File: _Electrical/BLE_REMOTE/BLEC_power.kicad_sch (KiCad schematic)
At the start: 37 parts, among them J1 USBC, J4 Battery, Q1 RE1C002UNTCL, Q2 IRLML6244, SW1 SW_Push, U2 BQ24232RGTR, U3 MCP65R41, U4 MIC5528-3.3YMX-TR

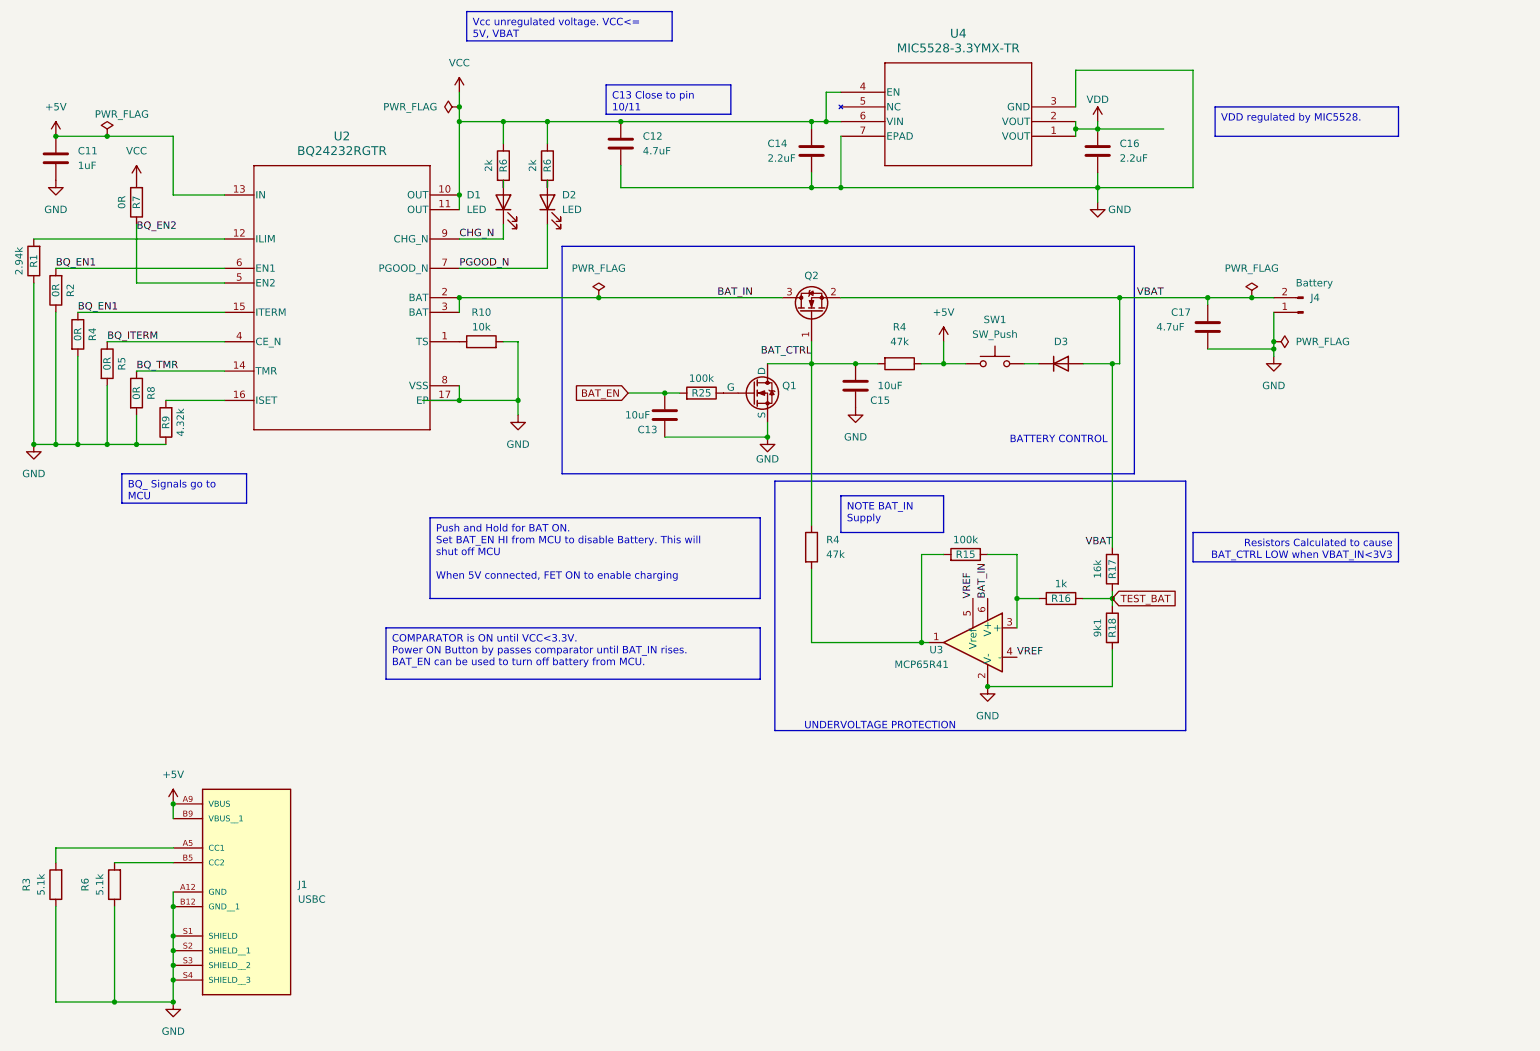
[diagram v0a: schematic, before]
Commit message: Added simulation and updated power button
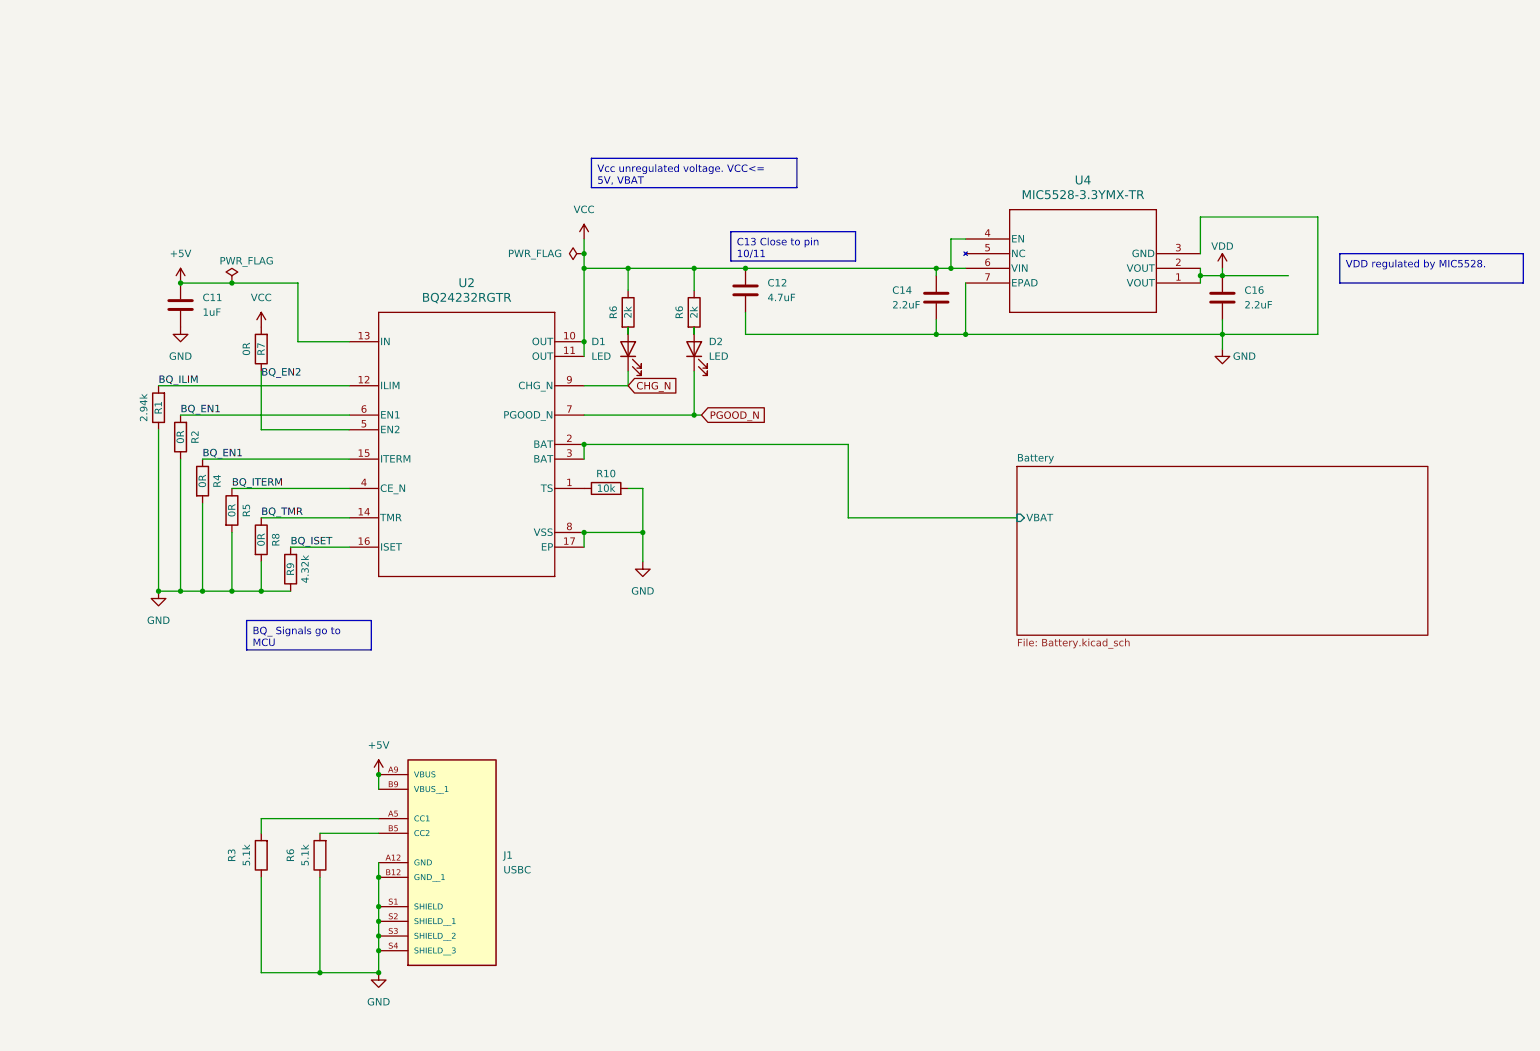
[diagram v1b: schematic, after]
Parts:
- removed C13, C15: 10uF, Capacitor_SMD:C_0402_1005Metric_Pad0.74x0.62mm_HandSolder, symbol Device:C
- removed C17: 4.7uF, Capacitor_SMD:C_0805_2012Metric_Pad1.18x1.45mm_HandSolder, symbol Device:C
- removed D3: 1N4148WX-TP, _Parts:CR_SOD323_MCC-L, symbol Device:D
- removed J4: Battery, _Parts:2pad_conn_sm, symbol Connector:Conn_01x02_Pin
- removed Q1: RE1C002UNTCL, _Parts:DIO_RB558WMF_ROM, symbol Simulation_SPICE:NMOS
- removed Q2: IRLML6244, Package_TO_SOT_SMD:SOT-23, symbol Transistor_FET:IRLML6244
- removed R15, R25: 100k, Resistor_SMD:R_0402_1005Metric_Pad0.72x0.64mm_HandSolder, symbol Device:R
- removed R16: 1k, Resistor_SMD:R_0402_1005Metric_Pad0.72x0.64mm_HandSolder, symbol Device:R
- removed R17: 16k, Resistor_SMD:R_0402_1005Metric_Pad0.72x0.64mm_HandSolder, symbol Device:R
- removed R18: 9k1, Resistor_SMD:R_0402_1005Metric_Pad0.72x0.64mm_HandSolder, symbol Device:R
- removed R4 (x2): 47k, Resistor_SMD:R_0402_1005Metric_Pad0.72x0.64mm_HandSolder, symbol Device:R
- removed SW1: SW_Push, symbol Switch:SW_Push
- removed U3: MCP65R41, Package_TO_SOT_SMD:SOT-23-6, symbol Comparator:MCP65R41
- J1: footprint USB4125-GF-A_REVA2:GCT_USB4125-GF-A_REVA2 -> _Parts:GCT_USB4125-GF-A_REVA2
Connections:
- net BQ_ISET: now reaches R9.2, U2.16 (ISET)
- net BQ_ILIM: now reaches R1.2, U2.12 (ILIM)
- net BAT_IN renamed Battery/VBAT
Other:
- added sheet Battery (Battery.kicad_sch)
- note removed: "BATTERY CONTROL"
- note removed: "UNDERVOLTAGE PROTECTION"
- moved on the sheet: C11, C12, C14, C16, D1, D2, J1, R1, R10, R2, R3, R4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

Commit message: started PCB design
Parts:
- removed J1: USBC, _Parts:GCT_USB4125-GF-A_REVA2, symbol USB4125-GF-A_REVA2:USB4125-GF-A_REVA2
- removed R3, R6: 5.1k, Resistor_SMD:R_0402_1005Metric_Pad0.72x0.64mm_HandSolder, symbol Device:R
- renumbered C14 to C13, C16 to C14, R4 to R3, R5 to R4, R7 to R5, R8 to R6, R9 to R7, U4 to U3
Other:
- added sheet USBC (USBC.kicad_sch)
- moved on the sheet: R10

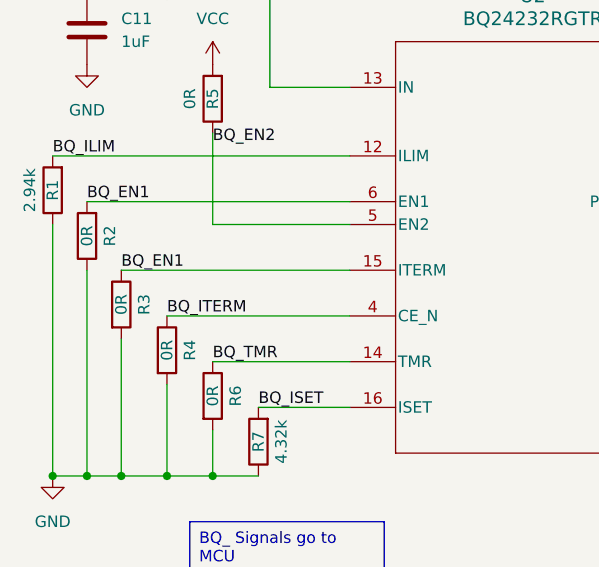
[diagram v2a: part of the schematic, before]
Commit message: PCB parts placed
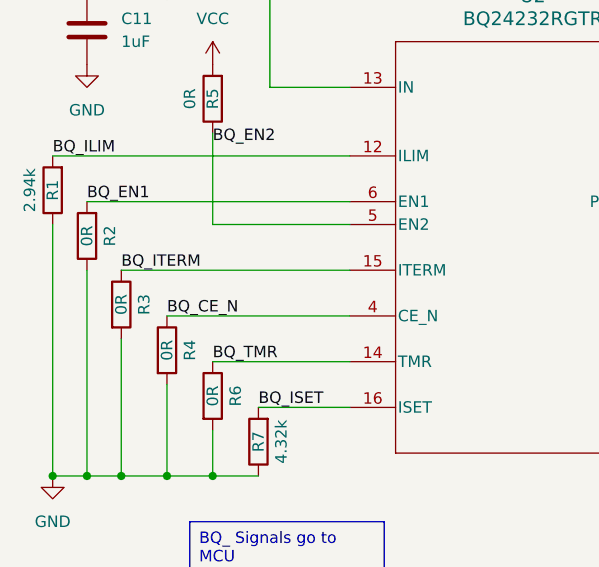
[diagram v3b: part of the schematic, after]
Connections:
- net BQ_EN1: no longer R3.1, U2.15 (ITERM)
- net BQ_ITERM: now also R3.1, U2.15 (ITERM); no longer R4.1, U2.4 (CE_N)
- new net BQ_CE_N: R4.1, U2.4 (CE_N)
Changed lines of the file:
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@@
     (effects (font (size 1.27 1.27)) (justify left bottom))
   )
-  (label "BQ_ITERM" (at 54.61 100.33 0) (fields_autoplaced)
+  (label "BQ_CE_N" (at 54.61 100.33 0) (fields_autoplaced)
     (effects (font (size 1.27 1.27)) (justify left bottom))
   )
@@
     (effects (font (size 1.27 1.27)) (justify left bottom))
   )
-  (label "BQ_EN1" (at 49.53 95.25 0) (fields_autoplaced)
+  (label "BQ_ITERM" (at 49.53 95.25 0) (fields_autoplaced)
     (effects (font (size 1.27 1.27)) (justify left bottom))
   )
@@
       (effects (font (size 1.27 1.27)) hide)
     )
+    (pin "3")
+    (pin "4")
     (pin "5")
-    (pin "4")
-    (pin "3")
-    (pin "1")
-    (pin "2")
     (pin "6")
+    (pin "1")
+    (pin "2")
     (pin "7")
     (instances

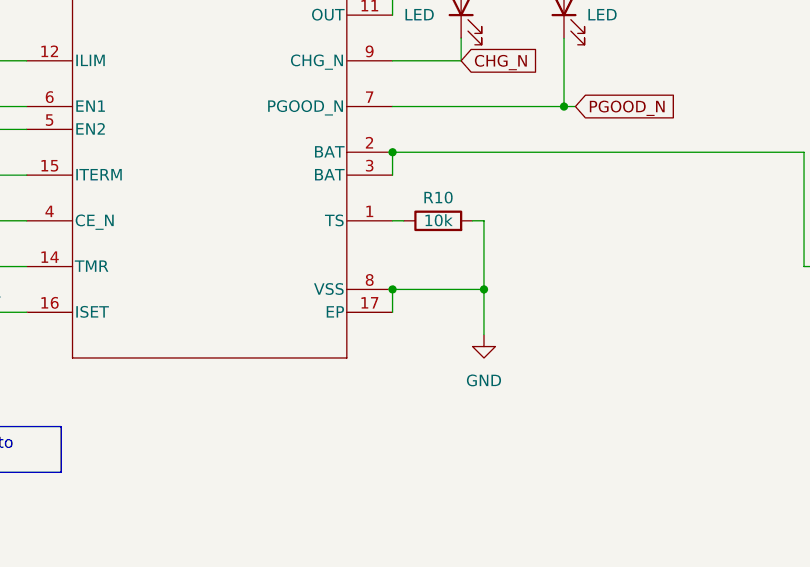
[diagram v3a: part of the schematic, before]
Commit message: Finished initial PCB draft
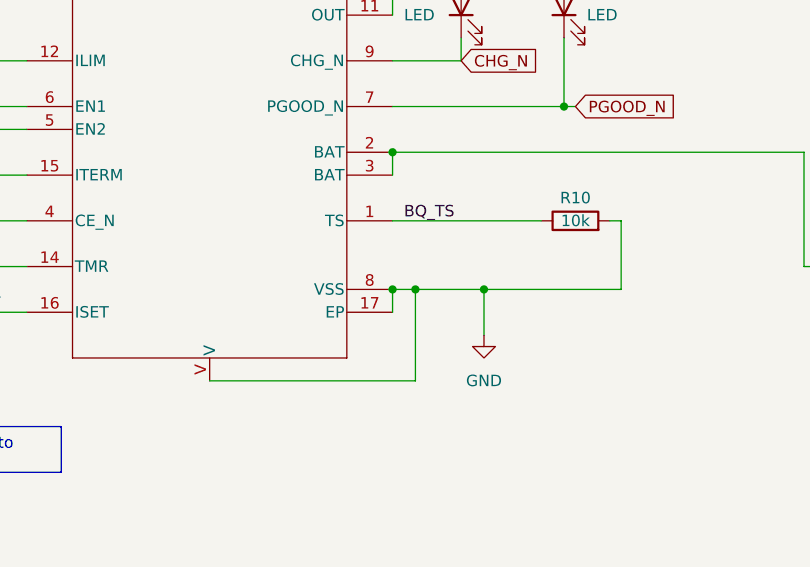
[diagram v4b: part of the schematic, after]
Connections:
- net GND: now also U2.V
- net BQ_TS: now reaches R10.1, U2.1 (TS)
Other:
- moved on the sheet: R10
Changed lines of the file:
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@@
   (junction (at 134.62 62.23) (diameter 0) (color 0 0 0 0)
   )
+  (junction (at 118.11 107.95) (diameter 0) (color 0 0 0 0)
+  )
   (junction (at 45.72 118.11) (diameter 0) (color 0 0 0 0)
   )
@@
   (junction (at 226.06 63.5) (diameter 0) (color 0 0 0 0)
   )
-  (wire (pts (xy 125.73 100.33) (xy 125.73 107.95))
+  (wire (pts (xy 140.97 100.33) (xy 140.97 107.95))
     (stroke (width 0) (type default))
   )
@@
     (stroke (width 0) (type default))
   )
-  (wire (pts (xy 116.84 100.33) (xy 115.57 100.33))
-    (stroke (width 0) (type default))
-  )
   (wire (pts (xy 125.73 107.95) (xy 125.73 113.03))
     (stroke (width 0) (type default))
@@
     (stroke (width 0) (type default))
   )
-  (wire (pts (xy 115.57 107.95) (xy 125.73 107.95))
+  (wire (pts (xy 115.57 107.95) (xy 118.11 107.95))
     (stroke (width 0) (type default))
   )
@@
     (stroke (width 0) (type default))
   )
+  (wire (pts (xy 118.11 118.11) (xy 118.11 107.95))
+    (stroke (width 0) (type default))
+  )
   (wire (pts (xy 115.57 74.93) (xy 115.57 77.47))
     (stroke (width 0) (type default))
@@
     (stroke (width 0) (type default))
   )
+  (wire (pts (xy 118.11 107.95) (xy 125.73 107.95))
+    (stroke (width 0) (type default))
+  )
   (wire (pts (xy 226.06 73.66) (xy 226.06 76.2))
     (stroke (width 0) (type default))
   )
+  (wire (pts (xy 95.25 118.11) (xy 118.11 118.11))
+    (stroke (width 0) (type default))
+  )
+  (wire (pts (xy 115.57 100.33) (xy 132.08 100.33))
+    (stroke (width 0) (type default))
+  )
   (wire (pts (xy 66.04 64.77) (xy 66.04 74.93))
     (stroke (width 0) (type default))
@@
     (stroke (width 0) (type default))
   )
+  (wire (pts (xy 140.97 107.95) (xy 125.73 107.95))
+    (stroke (width 0) (type default))
+  )
   (wire (pts (xy 242.57 73.66) (xy 226.06 73.66))
     (stroke (width 0) (type default))
@@
     (stroke (width 0) (type default))
   )
-  (wire (pts (xy 124.46 100.33) (xy 125.73 100.33))
+  (wire (pts (xy 139.7 100.33) (xy 140.97 100.33))
     (stroke (width 0) (type default))
   )
@@
   )
   (label "BQ_EN1" (at 45.72 87.63 0) (fields_autoplaced)
+    (effects (font (size 1.27 1.27)) (justify left bottom))
+  )
+  (label "BQ_TS" (at 116.84 100.33 0) (fields_autoplaced)
     (effects (font (size 1.27 1.27)) (justify left bottom))
   )
@@
     )
   )
-  (netclass_flag "" (length 2.54) (shape round) (at 114.3 100.33 0) (fields_autoplaced)
-    (effects (font (size 1.27 1.27)) (justify left bottom))
-    (property "Netclass" "Signal" (at 114.9985 97.79 0)
+  (netclass_flag "" (length 2.54) (shape round) (at 127 100.33 0) (fields_autoplaced)
+    (effects (font (size 1.27 1.27)) (justify left bottom))
+    (property "Netclass" "Signal" (at 127.6985 97.79 0)
       (effects (font (size 1.27 1.27) italic) (justify left))
     )
@@
     )
   )
-  (symbol (lib_id "Device:R") (at 120.65 100.33 90) (unit 1)
-    (in_bom yes) (on_board yes) (dnp no)
-    (property "Reference" "R10" (at 120.65 97.79 90)
-      (effects (font (size 1.27 1.27)))
-    )
-    (property "Value" "10k" (at 120.65 100.33 90)
-      (effects (font (size 1.27 1.27)))
-    )
-    (property "Footprint" "Resistor_SMD:R_0402_1005Metric_Pad0.72x0.64mm_HandSolder" (at 120.65 102.108 90)
-      (effects (font (size 1.27 1.27)) hide)
-    )
-    (property "Datasheet" "~" (at 120.65 100.33 0)
-      (effects (font (size 1.27 1.27)) hide)
-    )
-    (property "DIGIKEY" "" (at 120.65 100.33 0)
-      (effects (font (size 1.27 1.27)) hide)
-    )
-    (property "Part" "RC0402JR-0710KL" (at 120.65 100.33 0)
+  (symbol (lib_id "Device:R") (at 135.89 100.33 90) (unit 1)
+    (in_bom yes) (on_board yes) (dnp no)
+    (property "Reference" "R10" (at 135.89 97.79 90)
+      (effects (font (size 1.27 1.27)))
+    )
+    (property "Value" "10k" (at 135.89 100.33 90)
+      (effects (font (size 1.27 1.27)))
+    )
+    (property "Footprint" "Resistor_SMD:R_0402_1005Metric_Pad0.72x0.64mm_HandSolder" (at 135.89 102.108 90)
+      (effects (font (size 1.27 1.27)) hide)
+    )
+    (property "Datasheet" "~" (at 135.89 100.33 0)
+      (effects (font (size 1.27 1.27)) hide)
+    )
+    (property "DIGIKEY" "" (at 135.89 100.33 0)
+      (effects (font (size 1.27 1.27)) hide)
+    )
+    (property "Part" "RC0402JR-0710KL" (at 135.89 100.33 0)
       (effects (font (size 1.27 1.27)) hide)
     )
@@
   )
   (symbol (lib_id "2023-11-13_13-42-39:BQ24232RGTR") (at 95.25 92.71 0) (unit 1)
-    (in_bom yes) (on_board yes) (dnp no) (fields_autoplaced)
+    (in_bom yes) (on_board yes) (dnp no)
     (property "Reference" "U2" (at 95.25 64.77 0)
       (effects (font (size 1.524 1.524)))
@@
     (pin "8")
     (pin "9")
-    (instances
-      (project "BLE_REMOTE"
+    (pin "V")
+    (instances
+      (project "BLE_REMOTE"

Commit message: second iteration PCB layout
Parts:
- added J6: LED, _Parts:3pad_conn, symbol Connector:Conn_01x03_Pin
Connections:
- net +5V: now also J6.3 (Pin_3)
- net GND: now also J6.1 (Pin_1)
- new net TEST_BAT: J6.2 (Pin_2)
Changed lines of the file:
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@@
+    )
+  )
+  (global_label "TEST_BAT" (shape input) (at 97.79 163.83 180) (fields_autoplaced)
+    (effects (font (size 1.27 1.27)) (justify right))
+    (property "Intersheetrefs" "${INTERSHEET_REFS}" (at 86.2173 163.83 0)
+      (effects (font (size 1.27 1.27)) (justify right) hide)
     )
   )
@@
     )
   )
+  (symbol (lib_id "power:+5V") (at 97.79 161.29 0) (unit 1)
+    (in_bom yes) (on_board yes) (dnp no) (fields_autoplaced)
+    (property "Reference" "#PWR039" (at 97.79 165.1 0)
+      (effects (font (size 1.27 1.27)) hide)
+    )
+    (property "Value" "+5V" (at 97.79 156.21 0)
+      (effects (font (size 1.27 1.27)))
+    )
+    (property "Footprint" "" (at 97.79 161.29 0)
+      (effects (font (size 1.27 1.27)) hide)
+    )
+    (property "Datasheet" "" (at 97.79 161.29 0)
+      (effects (font (size 1.27 1.27)) hide)
+    )
+    (pin "1")
+    (instances
+      (project "BLE_REMOTE"
+        (path "/3c7105d6-b2e1-4841-966d-0562ae88783f/df7514b4-387c-47b1-a1bd-e93660408c5b"
+          (reference "#PWR039") (unit 1)
+        )
+      )
+    )
+  )
   (symbol (lib_id "power:GND") (at 226.06 76.2 0) (unit 1)
     (in_bom yes) (on_board yes) (dnp no)
@@
     )
   )
+  (symbol (lib_id "power:GND") (at 97.79 166.37 0) (unit 1)
+    (in_bom yes) (on_board yes) (dnp no) (fields_autoplaced)
+    (property "Reference" "#PWR040" (at 97.79 172.72 0)
+      (effects (font (size 1.27 1.27)) hide)
+    )
+    (property "Value" "GND" (at 97.79 171.45 0)
+      (effects (font (size 1.27 1.27)))
+    )
+    (property "Footprint" "" (at 97.79 166.37 0)
+      (effects (font (size 1.27 1.27)) hide)
+    )
+    (property "Datasheet" "" (at 97.79 166.37 0)
+      (effects (font (size 1.27 1.27)) hide)
+    )
+    (pin "1")
+    (instances
+      (project "BLE_REMOTE"
+        (path "/3c7105d6-b2e1-4841-966d-0562ae88783f/df7514b4-387c-47b1-a1bd-e93660408c5b"
+          (reference "#PWR040") (unit 1)
+        )
+      )
+    )
+  )
   (symbol (lib_id "Device:C") (at 176.53 67.31 0) (unit 1)
     (in_bom yes) (on_board yes) (dnp no)
@@
         )
       )
+    )
+  )
+  (symbol (lib_id "Connector:Conn_01x03_Pin") (at 102.87 163.83 180) (unit 1)
+    (in_bom yes) (on_board yes) (dnp no) (fields_autoplaced)
+    (property "Reference" "J6" (at 104.14 162.56 0)
+      (effects (font (size 1.27 1.27)) (justify right))
+    )
+    (property "Value" "LED" (at 104.14 165.1 0)
+      (effects (font (size 1.27 1.27)) (justify right))
+    )
+    (property "Footprint" "_Parts:3pad_conn" (at 102.87 163.83 0)
+      (effects (font (size 1.27 1.27)) hide)
+    )
+    (property "Datasheet" "~" (at 102.87 163.83 0)
+      (effects (font (size 1.27 1.27)) hide)
+    )
+    (pin "1")
+    (pin "2")
+    (pin "3")
+    (instances
+      (project "BLE_REMOTE"
+        (path "/3c7105d6-b2e1-4841-966d-0562ae88783f/df7514b4-387c-47b1-a1bd-e93660408c5b"
+          (reference "J6") (unit 1)
+        )
+      )

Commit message: finished initial PCB draft
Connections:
- net TEST_BAT renamed LED_D
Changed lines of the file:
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@@
     )
   )
-  (global_label "TEST_BAT" (shape input) (at 97.79 163.83 180) (fields_autoplaced)
+  (global_label "LED_D" (shape input) (at 97.79 163.83 180) (fields_autoplaced)
     (effects (font (size 1.27 1.27)) (justify right))
-    (property "Intersheetrefs" "${INTERSHEET_REFS}" (at 86.2173 163.83 0)
+    (property "Intersheetrefs" "${INTERSHEET_REFS}" (at 89.1995 163.83 0)
       (effects (font (size 1.27 1.27)) (justify right) hide)
     )
